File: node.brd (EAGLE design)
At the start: 50 x 68.5 mm, 12 parts, among them J1 RJ11, J2 RJ11

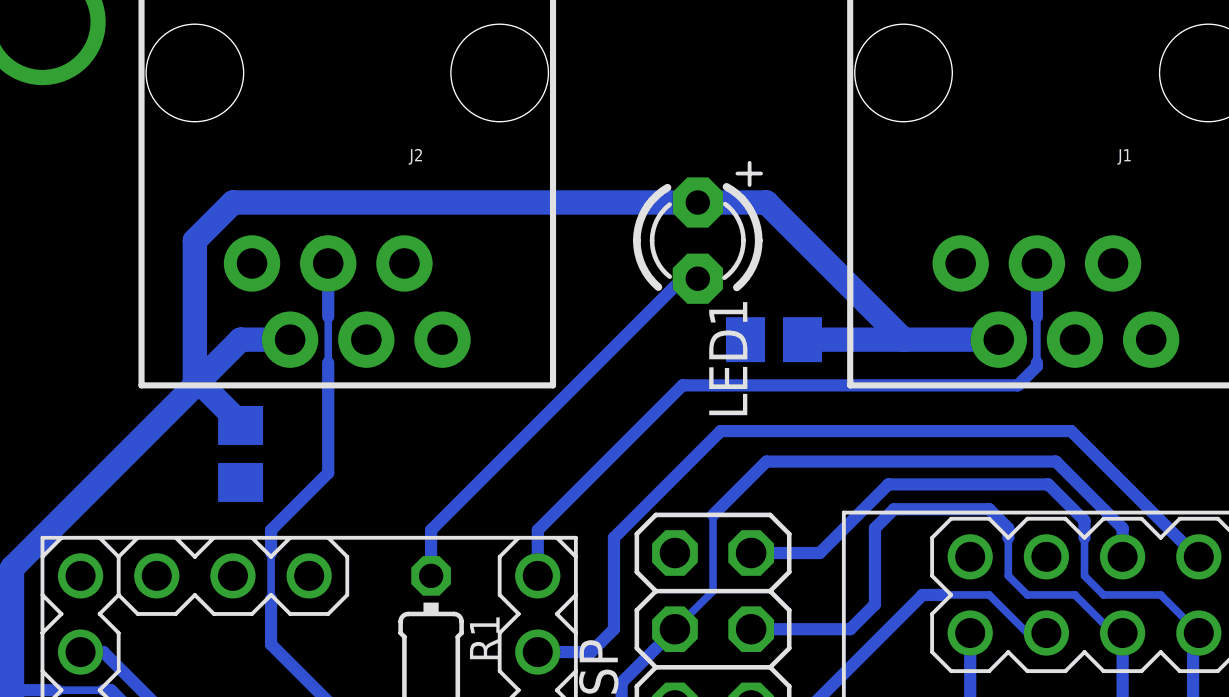
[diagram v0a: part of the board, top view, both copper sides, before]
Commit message: Added 10k pull-up resistors.
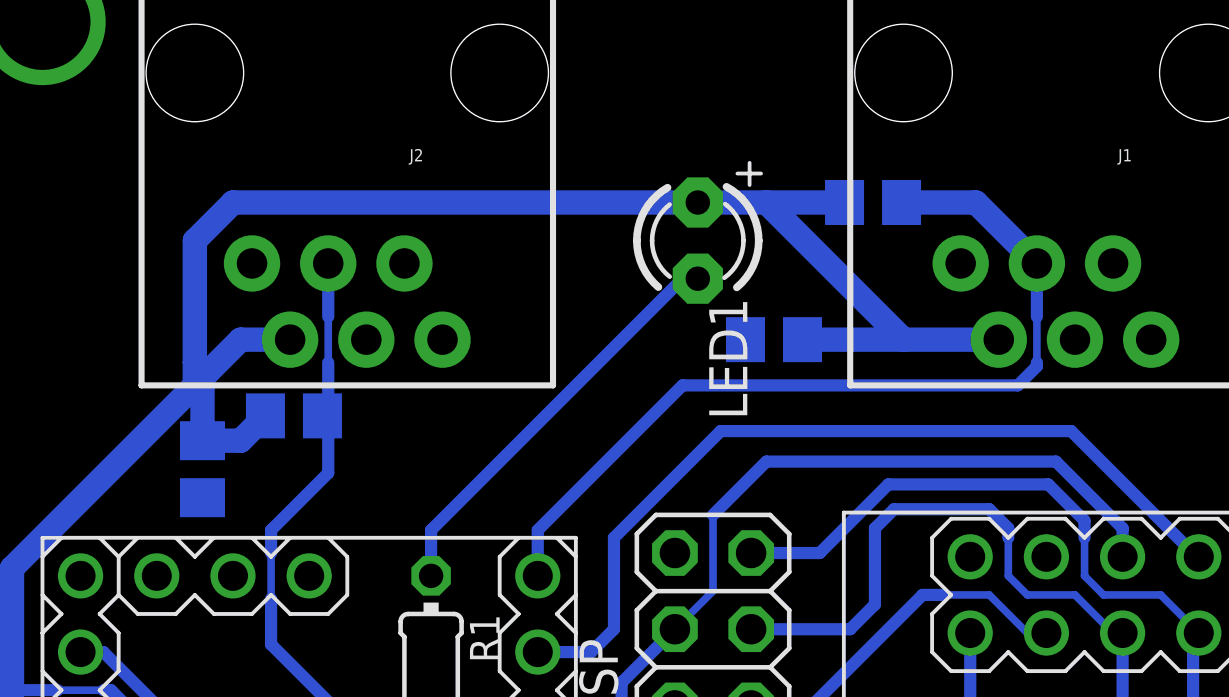
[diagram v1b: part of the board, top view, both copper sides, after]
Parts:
- added R2, R3: 10k, rcl:R0805
- moved C2 1.37 mm to (8.38, 50.5)
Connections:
- net +5V: now also R2.2, R3.2
- net DHT0_SIG: now also R2.1
- net DHT1_SIG: now also R3.1
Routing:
- net +5V: track 109.4 -> 115.3 mm
- net DHT0_SIG: track 23.9 -> 29.2 mm
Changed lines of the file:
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@@
 <element name="LED1" library="adafruit" package="LED3MM" value="" x="24.892" y="58.166" rot="R270"/>
 <element name="R1" library="rcl" package="0204/7" value="" x="16.002" y="43.18" rot="R270"/>
-<element name="C2" library="rcl" package="C0805" value="100nF" x="9.652" y="51.054" rot="MR270"/>
+<element name="C2" library="rcl" package="C0805" value="100nF" x="8.382" y="50.546" rot="MR270"/>
 <element name="C3" library="rcl" package="C0805" value="100nF" x="27.432" y="54.864" rot="MR0"/>
 <element name="C1" library="rcl" package="E2,5-6" value="" x="24.638" y="9.144" rot="R270"/>
+<element name="R2" library="rcl" package="R0805" value="10k" x="30.734" y="59.436" rot="MR0"/>
+<element name="R3" library="rcl" package="R0805" value="10k" x="11.43" y="52.324" rot="MR0"/>
 </elements>
 <signals>
@@
 <wire x1="12.573" y1="57.404" x2="12.573" y2="55.626" width="0.4064" layer="16"/>
 <wire x1="12.573" y1="55.626" x2="12.573" y2="54.102" width="0.254" layer="16"/>
-<wire x1="12.573" y1="54.102" x2="12.573" y2="50.419" width="0.4064" layer="16"/>
+<wire x1="12.573" y1="54.102" x2="12.573" y2="52.578" width="0.4064" layer="16"/>
+<wire x1="12.573" y1="52.578" x2="12.573" y2="50.419" width="0.4064" layer="16"/>
 <wire x1="12.573" y1="50.419" x2="10.668" y2="48.514" width="0.4064" layer="16"/>
+<contactref element="R3" pad="1"/>
+<wire x1="12.38" y1="52.324" x2="12.38" y2="52.385" width="0.6096" layer="16"/>
+<wire x1="12.38" y1="52.385" x2="12.573" y2="52.578" width="0.6096" layer="16"/>
 </signal>
 <signal name="DHT0_SIG">
@@
 <wire x1="36.195" y1="55.626" x2="36.195" y2="54.102" width="0.254" layer="16"/>
 <wire x1="36.195" y1="54.102" x2="36.195" y2="53.975" width="0.4064" layer="16"/>
+<wire x1="19.558" y1="48.514" x2="19.558" y2="46.99" width="0.4064" layer="16"/>
+<contactref element="R2" pad="1"/>
 <wire x1="36.195" y1="53.975" x2="35.56" y2="53.34" width="0.4064" layer="16"/>
 <wire x1="35.56" y1="53.34" x2="24.384" y2="53.34" width="0.4064" layer="16"/>
 <wire x1="24.384" y1="53.34" x2="19.558" y2="48.514" width="0.4064" layer="16"/>
-<wire x1="19.558" y1="48.514" x2="19.558" y2="46.99" width="0.4064" layer="16"/>
+<wire x1="31.684" y1="59.436" x2="34.163" y2="59.436" width="0.8128" layer="16"/>
+<wire x1="34.163" y1="59.436" x2="36.195" y2="57.404" width="0.8128" layer="16"/>
 </signal>
 <signal name="+3V3">
@@
 <wire x1="13.716" y1="33.02" x2="18.796" y2="33.02" width="0.4064" layer="16"/>
 <wire x1="2.032" y1="47.244" x2="8.128" y2="53.34" width="0.8128" layer="16"/>
-<wire x1="8.128" y1="53.34" x2="8.128" y2="58.166" width="0.8128" layer="16"/>
+<wire x1="8.128" y1="53.34" x2="8.128" y2="54.102" width="0.8128" layer="16"/>
+<wire x1="8.128" y1="54.102" x2="8.128" y2="58.166" width="0.8128" layer="16"/>
 <wire x1="8.128" y1="58.166" x2="9.398" y2="59.436" width="0.8128" layer="16"/>
 <wire x1="9.398" y1="59.436" x2="24.892" y2="59.436" width="0.8128" layer="16"/>
@@
 <wire x1="31.75" y1="54.864" x2="34.925" y2="54.864" width="0.8128" layer="16"/>
 <wire x1="11.303" y1="54.864" x2="9.652" y2="54.864" width="0.8128" layer="16"/>
-<wire x1="9.652" y1="54.864" x2="8.255" y2="53.467" width="0.8128" layer="16"/>
+<wire x1="9.652" y1="54.864" x2="8.509" y2="53.721" width="0.8128" layer="16"/>
 <contactref element="C2" pad="1"/>
 <contactref element="C3" pad="1"/>
-<wire x1="8.255" y1="53.467" x2="8.128" y2="53.34" width="0.8128" layer="16"/>
+<wire x1="8.509" y1="53.721" x2="8.128" y2="53.34" width="0.8128" layer="16"/>
 <wire x1="28.382" y1="54.864" x2="31.75" y2="54.864" width="0.8128" layer="16"/>
-<wire x1="9.652" y1="52.004" x2="9.652" y2="52.07" width="0.8128" layer="16"/>
-<wire x1="9.652" y1="52.07" x2="8.255" y2="53.467" width="0.8128" layer="16"/>
+<contactref element="R2" pad="2"/>
+<contactref element="R3" pad="2"/>
+<wire x1="8.382" y1="53.594" x2="8.509" y2="53.721" width="0.6096" layer="16"/>
+<wire x1="8.382" y1="51.496" x2="8.382" y2="53.848" width="0.8128" layer="16"/>
+<wire x1="8.382" y1="53.848" x2="8.128" y2="54.102" width="0.8128" layer="16"/>
+<wire x1="8.382" y1="51.496" x2="9.652" y2="51.496" width="0.8128" layer="16"/>
+<wire x1="9.652" y1="51.496" x2="10.48" y2="52.324" width="0.8128" layer="16"/>
+<wire x1="27.178" y1="59.436" x2="29.784" y2="59.436" width="0.8128" layer="16"/>
 </signal>
 <signal name="ENC28J60_DATA_INT">
